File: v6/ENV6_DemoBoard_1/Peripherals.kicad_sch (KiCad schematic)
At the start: 34 parts, among them J201 MEM2052-00-195-00-A, U201 PAC1954x-x4MX, U202 PAC1954x-x4MX, U203 PAC1954x-x4MX

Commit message: SPartan7Board and new Symbol and Footprint
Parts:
- C201, C203, C205, C208: value 10u -> 1u
- C202, C204, C206, C207: value 100n -> 1u
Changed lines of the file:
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@@
 			)
 		)
-		(property "Value" "100n"
+		(property "Value" "1u"
 			(at 117.348 49.53 0)
 			(show_name no)
@@
 			)
 		)
-		(property "Value" "10u"
+		(property "Value" "1u"
 			(at 104.648 158.75 0)
 			(show_name no)
@@
 			)
 		)
-		(property "Value" "100n"
+		(property "Value" "1u"
 			(at 144.018 72.39 0)
 			(show_name no)
@@
 			)
 		)
-		(property "Value" "10u"
+		(property "Value" "1u"
 			(at 156.718 72.39 0)
 			(show_name no)
@@
 			)
 		)
-		(property "Value" "10u"
+		(property "Value" "1u"
 			(at 105.918 49.53 0)
 			(show_name no)
@@
 			)
 		)
-		(property "Value" "10u"
+		(property "Value" "1u"
 			(at 105.918 111.76 0)
 			(show_name no)
@@
 			)
 		)
-		(property "Value" "100n"
+		(property "Value" "1u"
 			(at 117.348 111.76 0)
 			(show_name no)
@@
 			)
 		)
-		(property "Value" "100n"
+		(property "Value" "1u"
 			(at 116.078 158.75 0)
 			(show_name no)

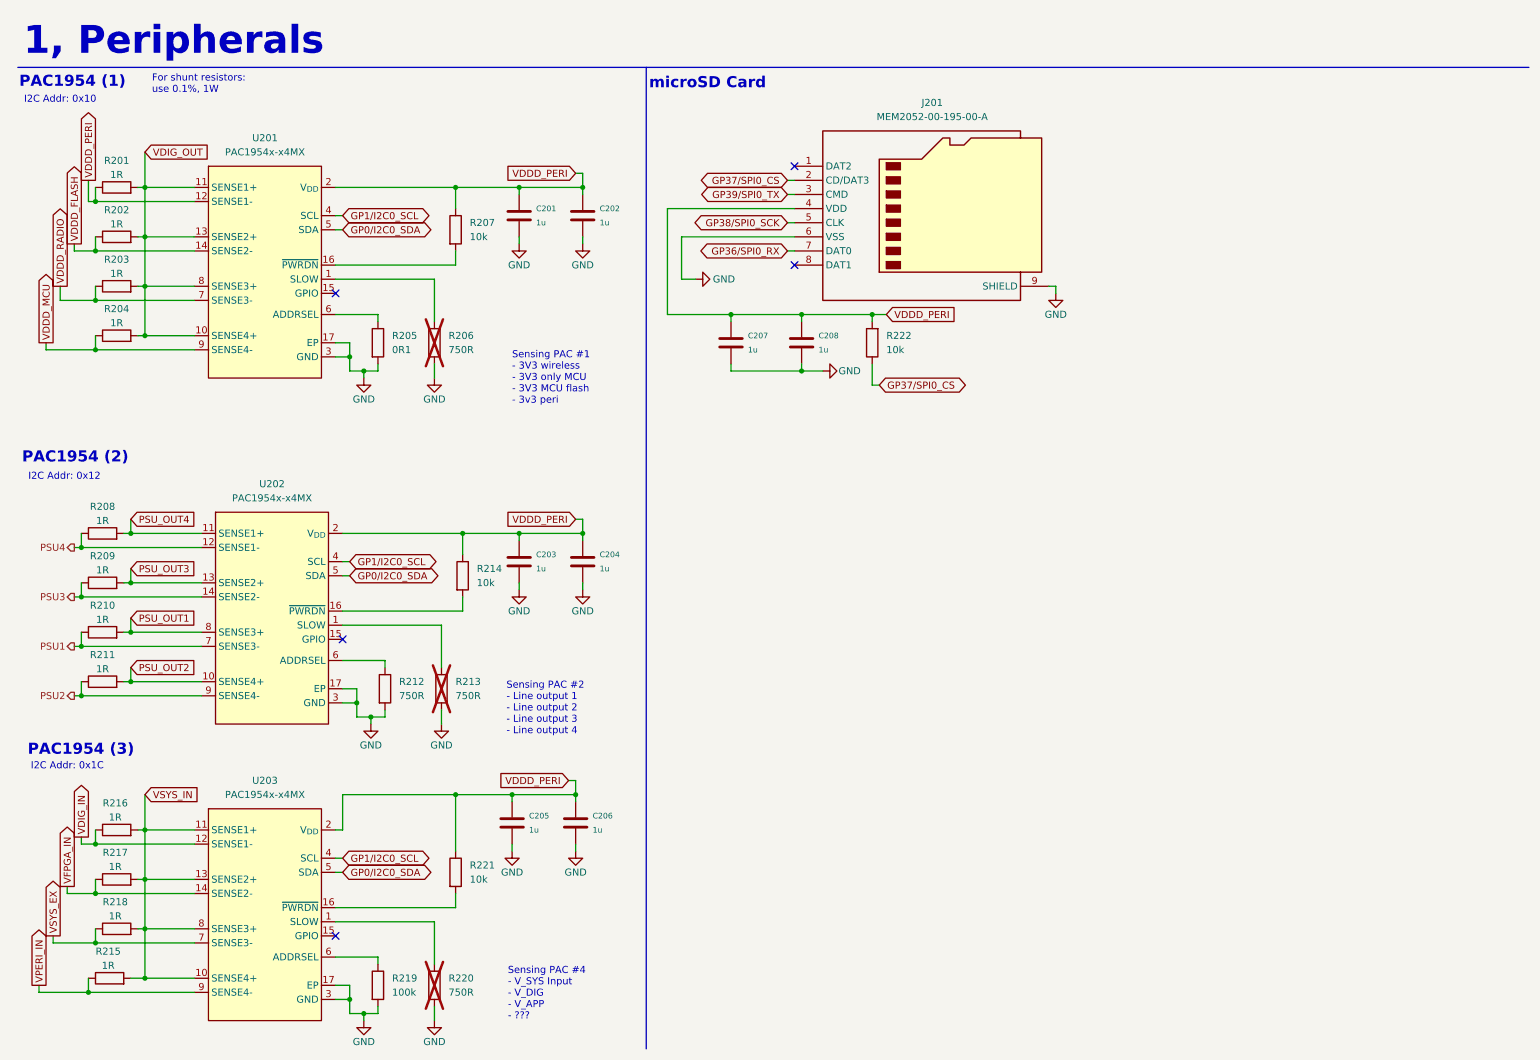
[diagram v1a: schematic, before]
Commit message: update measurement for PPK2
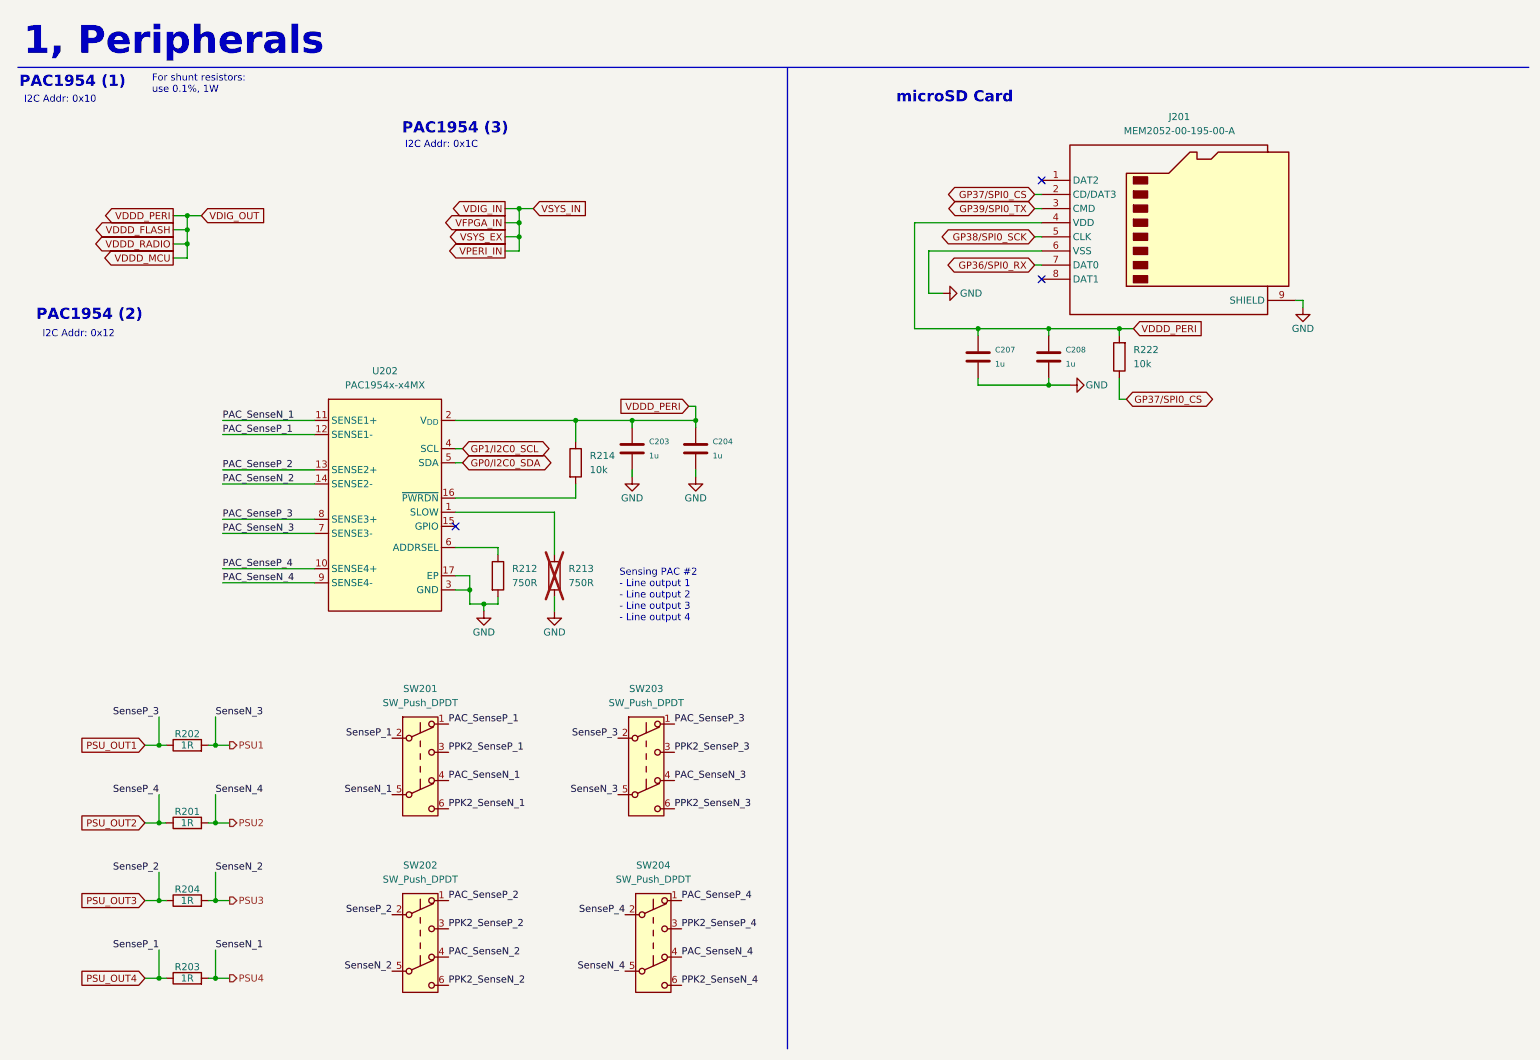
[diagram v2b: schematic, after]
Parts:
- removed C201, C202, C205, C206: 1u, Capacitor_SMD:C_0402_1005Metric, symbol passive:C0402
- removed R205: 0R1, Resistor_SMD:R_0402_1005Metric, symbol passive:R0402
- removed R206, R220: 750R, Resistor_SMD:R_0402_1005Metric, symbol passive:R0402
- removed R207, R221: 10k, Resistor_SMD:R_0402_1005Metric, symbol passive:R0402
- removed R208, R209, R210, R211, R215, R216, R217, R218: 1R, Resistor_SMD:R_0603_1608Metric, symbol passive:R0402
- removed R219: 100k, Resistor_SMD:R_0402_1005Metric, symbol passive:R0402
- removed U201, U203: PAC1954x-x4MX, Package_DFN_QFN:VQFN-16-1EP_3x3mm_P0.5mm_EP1.1x1.1mm, symbol sensors:PAC1954x-x4MX
- added SW201, SW202, SW203, SW204: SW_Push_DPDT, symbol Switch:SW_Push_DPDT
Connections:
- net VDDD_MCU is gone; now on net PSU_OUT3: R204.1
- net VDDD_RADIO is gone; now on net PSU_OUT4: R203.1
- net PSU1: now also R202.2, SW203.5 (B); no longer U202.7 (SENSE3-)
- net PSU2: now also R201.2, SW204.5 (B); no longer U202.9 (SENSE4-)
- net PSU3: now also R204.2, SW202.5 (B); no longer U202.14 (SENSE2-)
- net PSU4: now also R203.2, SW201.5 (B); no longer U202.12 (SENSE1-)
- net PSU_OUT1: now also R202.1, SW203.2 (B); no longer U202.8 (SENSE3+)
- net PSU_OUT2: now also R201.1, SW204.2 (B); no longer U202.10 (SENSE4+)
- net PSU_OUT3: now also SW202.2 (B); no longer U202.13 (SENSE2+)
- net PSU_OUT4: now also SW201.2 (B); no longer U202.11 (SENSE1+)
- net VDDD_FLASH: now also C203.2, C204.2, C207.2, C208.2, J201.4 (VDD), R214.1, R222.2, U202.2 (V_{DD}); no longer R202.1
- removed net VDDD_PERI: C203.2, C204.2, C207.2, C208.2, J201.4 (VDD), R201.1, R214.1, R222.2, U202.2 (V_{DD})
- removed net VDIG_OUT: R201.2, R202.2, R203.2, R204.2
- new net PAC_SenseN_1: SW201.4 (A), U202.11 (SENSE1+)
- new net PAC_SenseN_2: SW202.4 (A), U202.14 (SENSE2-)
- new net PAC_SenseN_3: SW203.4 (A), U202.7 (SENSE3-)
- new net PAC_SenseN_4: SW204.4 (A), U202.9 (SENSE4-)
- new net PAC_SenseP_1: SW201.1 (A), U202.12 (SENSE1-)
- new net PAC_SenseP_2: SW202.1 (A), U202.13 (SENSE2+)
- new net PAC_SenseP_3: SW203.1 (A), U202.8 (SENSE3+)
- new net PAC_SenseP_4: SW204.1 (A), U202.10 (SENSE4+)
- new net PPK2_SenseN_1: SW201.6 (C)
- new net PPK2_SenseN_2: SW202.6 (C)
- new net PPK2_SenseN_3: SW203.6 (C)
- new net PPK2_SenseN_4: SW204.6 (C)
- new net PPK2_SenseP_1: SW201.3 (C)
- new net PPK2_SenseP_2: SW202.3 (C)
- new net PPK2_SenseP_3: SW203.3 (C)
- new net PPK2_SenseP_4: SW204.3 (C)
- no-connect marks 5 -> 3
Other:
- note removed: "Sensing PAC #1 - 3V3 wireless - 3V3 only MCU - 3V3 MCU flash - 3v3 peri"
- note removed: "Sensing PAC #4 - V_SYS Input - V_DIG - V_APP - ???"
- moved on the sheet: C203, C204, C207, C208, J201, R212, R213, R214, R222, U202

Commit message: Fix small errors for the design
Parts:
- removed U202: PAC1954x-x4MX, Package_DFN_QFN:VQFN-16-1EP_3x3mm_P0.5mm_EP1.1x1.1mm, symbol sensors:PAC1954x-x4MX
- added U201: PAC1954T-E4Mx, sensors:VQFN-16-1EP_3x3mm_P0.5mm_EP1.1x1.1mm, symbol sensors:PAC1954T-E4Mx
- renumbered C203 to C201, C204 to C202, C207 to C203, C208 to C204, R202 to R201, R201 to R202, R204 to R203, R203 to R204, R212 to R205, R213 to R206, R214 to R207, R222 to R208
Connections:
- net GND: now also U201.17 (EP), U201.3 (GND)
- net GP0/I2C0_SDA: now also U201.5 (SDA)
- net GP1/I2C0_SCL: now also U201.4 (SCL)
- net PAC_SenseN_1: now also U201.11 (SENSE1+)
- net PAC_SenseN_2: now also U201.14 (SENSE2-)
- net PAC_SenseN_3: now also U201.7 (SENSE3-)
- net PAC_SenseN_4: now also U201.9 (SENSE4-)
- net PAC_SenseP_1: now also U201.12 (SENSE1-)
- net PAC_SenseP_2: now also U201.13 (SENSE2+)
- net PAC_SenseP_3: now also U201.8 (SENSE3+)
- net PAC_SenseP_4: now also U201.10 (SENSE4+)
- net VDDD_FLASH: now also U201.2 (V_{DD})
- net at R207.2: now also U201.16 (~{PWRDN})
- net at R205.1: now also U201.6 (ADDRSEL)
- net at R206.1: now also U201.1 (SLOW)
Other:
- moved on the sheet: R201, R202, R203, R204, SW201, SW202, SW203, SW204
